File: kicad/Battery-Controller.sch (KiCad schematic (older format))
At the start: 55 parts, among them J1 Screw_Terminal_01x04 - RELAY, J2 Screw_Terminal_01x04 - COM, J3 Screw_Terminal_01x08, J4 Screw_Terminal_01x02 - Batter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, J6 Screw_Terminal_01x04 - Cells, J7 Conn_01x15_Male, J8 Conn_01x15_Female, Q1 TIP120, Q2 TIP122, Q3 TIP122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

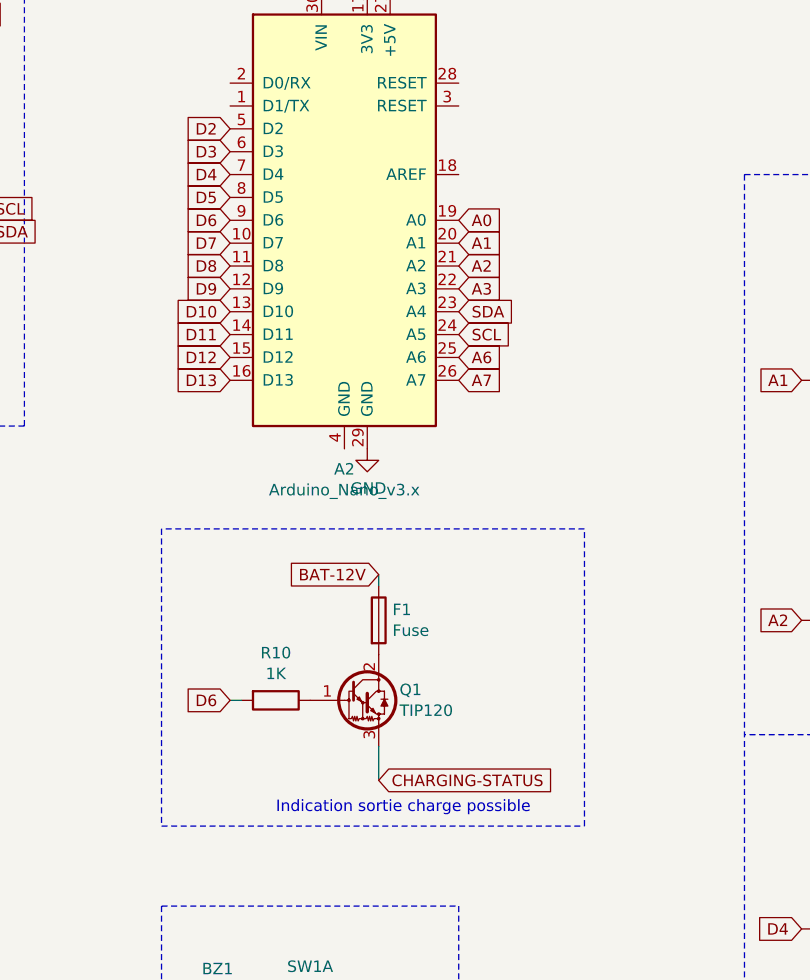
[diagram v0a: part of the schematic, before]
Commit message: Fonctionne, correctement réglé, NO serial transfer
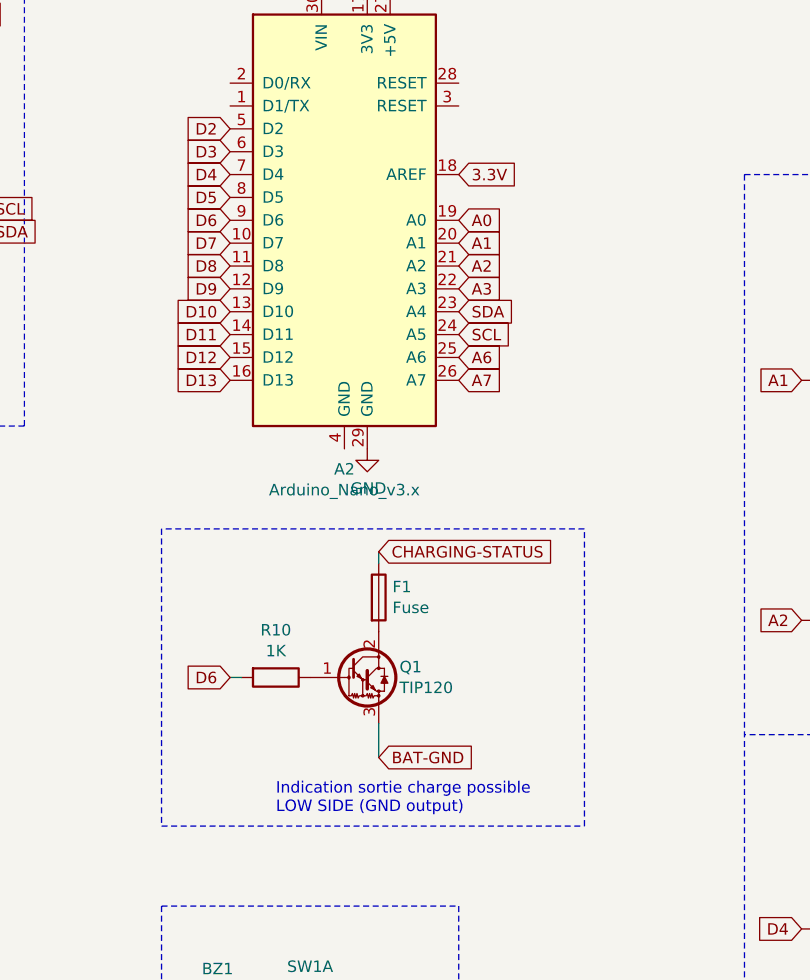
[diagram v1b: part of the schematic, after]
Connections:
- net +12V: no longer F1.1
- net 3.3V: now also A2.18 (AREF)
- net CHARGING-STATUS: now also F1.1; no longer Q1.3 (E)
- net GND: now also Q1.3 (E)
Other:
- note added: "Indication sortie charge possible\nLOW SIDE (GND output)\n"
- note removed: "Indication sortie charge possible\n"
- moved on the sheet: F1, Q1, R10
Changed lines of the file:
@@
 L Transistor_BJT:TIP120 Q1
 U 1 1 61B48AE2
-P 6750 6400
-F 0 "Q1" H 6941 6446 50  0000 L CNN
-F 1 "TIP120" H 6941 6355 50  0000 L CNN
-F 2 "Package_TO_SOT_THT:TO-220-3_Vertical" H 6950 6500 50  0001 C CNN
-F 3 "~" H 6750 6400 50  0001 C CNN
-	1    6750 6400
+P 6750 6300
+F 0 "Q1" H 6941 6346 50  0000 L CNN
+F 1 "TIP120" H 6941 6255 50  0000 L CNN
+F 2 "Package_TO_SOT_THT:TO-220-3_Vertical" H 6950 6400 50  0001 C CNN
+F 3 "~" H 6750 6300 50  0001 C CNN
+	1    6750 6300
 	1    0    0    -1
 $EndComp
@@
 L Device:R R10
 U 1 1 61B49F2F
-P 6400 6400
-F 0 "R10" V 6193 6400 50  0000 C CNN
-F 1 "1K" V 6284 6400 50  0000 C CNN
-F 2 "Resistor_THT:R_Axial_DIN0207_L6.3mm_D2.5mm_P10.16mm_Horizontal" V 6330 6400 50  0001 C CNN
-F 3 "~" H 6400 6400 50  0001 C CNN
-	1    6400 6400
+P 6400 6300
+F 0 "R10" V 6193 6300 50  0000 C CNN
+F 1 "1K" V 6284 6300 50  0000 C CNN
+F 2 "Resistor_THT:R_Axial_DIN0207_L6.3mm_D2.5mm_P10.16mm_Horizontal" V 6330 6300 50  0001 C CNN
+F 3 "~" H 6400 6300 50  0001 C CNN
+	1    6400 6300
 	0    1    1    0
 $EndComp
@@
 	5900 5650 5900 6950
 Text Notes 6400 6900 0    50   ~ 0
-Indication sortie charge possible\n
+Indication sortie charge possible\nLOW SIDE (GND output)\n
 $Comp
 L Device:Fuse F1
 U 1 1 61B5B3F4
-P 6850 6050
-F 0 "F1" H 6910 6096 50  0000 L CNN
-F 1 "Fuse" H 6910 6005 50  0000 L CNN
-F 2 "Fuse:Fuseholder_Blade_ATO_Littelfuse_Pudenz_2_Pin" V 6780 6050 50  0001 C CNN
-F 3 "~" H 6850 6050 50  0001 C CNN
-	1    6850 6050
-	1    0    0    -1
-$EndComp
-Wire Wire Line
-	6850 6600 6850 6750
-Text GLabel 6850 6750 2    50   Input ~ 0
+P 6850 5950
+F 0 "F1" H 6910 5996 50  0000 L CNN
+F 1 "Fuse" H 6910 5905 50  0000 L CNN
+F 2 "Fuse:Fuseholder_Blade_ATO_Littelfuse_Pudenz_2_Pin" V 6780 5950 50  0001 C CNN
+F 3 "~" H 6850 5950 50  0001 C CNN
+	1    6850 5950
+	1    0    0    -1
+$EndComp
+Wire Wire Line
+	6850 6500 6850 6650
+Text GLabel 6850 5750 2    50   Input ~ 0
 CHARGING-STATUS
 Wire Notes Line
@@
 Text GLabel 6200 4300 0    50   Input ~ 0
 D6
-Text GLabel 6200 6400 0    50   Input ~ 0
+Text GLabel 6200 6300 0    50   Input ~ 0
 D6
 Wire Wire Line
-	6250 6400 6200 6400
+	6250 6300 6200 6300
 $Comp
 L Connector:Screw_Terminal_01x04 J1
@@
 	1    0    0    -1
 $EndComp
-Text GLabel 6850 5850 0    50   Input ~ 0
-BAT-12V
-Wire Wire Line
-	6850 5850 6850 5900
+Text GLabel 6850 6650 2    50   Input ~ 0
+BAT-GND
+Wire Wire Line
+	6850 5750 6850 5800
 $Comp
 L yaaj_dcdc_stepdown_lm2596:YAAJ_DCDC_StepDown_LM2596 U1
@@
 Wire Wire Line
 	9400 8250 9300 8250
+Text GLabel 7200 4100 2    50   Input ~ 0
+3.3V
 $EndSCHEMATC

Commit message: RS484 included, not enough ram
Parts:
- removed BZ1: Buzzer, Buzzer_Beeper:Buzzer_12x9.5RM7.6, symbol Device:Buzzer
- removed SW1: SW_DPST_x2, Connector_PinHeader_2.54mm:PinHeader_1x02_P2.54mm_Vertical, symbol Switch:SW_DPST_x2
- added Arduino2: Arduino_Nano_v3.x, Module:Arduino_Nano, symbol Battery-Controller-rescue:Arduino_Nano_v3.x-MCU_Module
- added C?: 1.5uF, Capacitor_THT:C_Disc_D8.0mm_W5.0mm_P7.50mm, symbol Device:CP
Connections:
- net GND2: now also U4.2 (~RE), C?.2
- net UP-5V: now also C?.1
- net UP-D7: now also U4.3 (DE)
- net RS-485-OUT1 renamed RS-485-RX
- net RS-485-RX: now also U4.6 (A); no longer U4.7 (B)
- net RS-485-OUT2 renamed RS-485-TX
- net RS-485-TX: now also U4.7 (B); no longer U4.6 (A)
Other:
- note removed: "Buzzer\n"
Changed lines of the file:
@@
 Text GLabel 7200 4800 2    50   Input ~ 0
 SCL
-$Comp
-L Device:Buzzer BZ1
-U 1 1 61B2EC2C
-P 6150 7900
-F 0 "BZ1" H 6155 7575 50  0000 C CNN
-F 1 "Buzzer" H 6155 7666 50  0000 C CNN
-F 2 "Buzzer_Beeper:Buzzer_12x9.5RM7.6" V 6125 8000 50  0001 C CNN
-F 3 "~" V 6125 8000 50  0001 C CNN
-	1    6150 7900
-	-1   0    0    1
-$EndComp
-Text GLabel 6800 7800 2    50   Input ~ 0
-UP-D7
 Text GLabel 6200 4400 0    50   Input ~ 0
 D7
-$Comp
-L Switch:SW_DPST_x2 SW1
-U 1 1 61B4152C
-P 6550 7800
-F 0 "SW1" H 6550 8035 50  0000 C CNN
-F 1 "SW_DPST_x2" H 6550 7944 50  0000 C CNN
-F 2 "Connector_PinHeader_2.54mm:PinHeader_1x02_P2.54mm_Vertical" H 6550 7800 50  0001 C CNN
-F 3 "~" H 6550 7800 50  0001 C CNN
-	1    6550 7800
-	1    0    0    -1
-$EndComp
 $Comp
 L Transistor_BJT:TIP120 Q1
@@
 Text GLabel 6850 5750 2    50   Input ~ 0
 CHARGING-STATUS
-Wire Notes Line
-	7200 8250 5900 8250
-Wire Notes Line
-	5900 8250 5900 7300
-Wire Notes Line
-	5900 7300 7200 7300
-Wire Notes Line
-	7200 7300 7200 8250
-Text Notes 6850 8200 0    50   ~ 0
-Buzzer\n
 Text Notes 11350 8800 0    50   ~ 0
 LOAD relay\n
@@
 	3600 7400 3600 7350
 Wire Wire Line
-	4200 7350 3600 7350
+	4200 7350 4050 7350
 Connection ~ 3600 7350
 Text GLabel 3900 7850 2    50   Input ~ 0
-RS-485-OUT1
+RS-485-TX
 Text GLabel 3900 7950 2    50   Input ~ 0
-RS-485-OUT2
+RS-485-RX
 Text GLabel 9900 1650 0    50   Input ~ 0
-RS-485-OUT1
+RS-485-RX
 Text GLabel 9900 1750 0    50   Input ~ 0
-RS-485-OUT2
+RS-485-TX
 Text Notes 4100 8450 0    50   ~ 0
 RS-485 BUS
@@
 Text GLabel 9900 2050 0    50   Input ~ 0
 LOAD-RELAY-STATUS
-Wire Wire Line
-	6400 8000 6250 8000
-Wire Wire Line
-	6250 7800 6350 7800
-Wire Wire Line
-	6800 7800 6750 7800
 Text GLabel 9900 2550 0    50   Input ~ 0
 SOC-ENABLE
@@
 $EndComp
 $Comp
-L power:GND2 #PWR0126
-U 1 1 6214F46F
-P 3650 9550
-F 0 "#PWR0126" H 3650 9300 50  0001 C CNN
-F 1 "GND2" H 3655 9377 50  0000 C CNN
-F 2 "" H 3650 9550 50  0001 C CNN
-F 3 "" H 3650 9550 50  0001 C CNN
-	1    3650 9550
-	1    0    0    -1
-$EndComp
-Text GLabel 3400 9550 0    50   Input ~ 0
-TUP-01
-Wire Wire Line
-	3400 9550 3650 9550
-Text GLabel 3400 9350 0    50   Input ~ 0
-TUP-02
-$Comp
-L power:+5VD #PWR0127
-U 1 1 621617F9
-P 3650 9300
-F 0 "#PWR0127" H 3650 9150 50  0001 C CNN
-F 1 "+5VD" H 3665 9473 50  0000 C CNN
-F 2 "" H 3650 9300 50  0001 C CNN
-F 3 "" H 3650 9300 50  0001 C CNN
-	1    3650 9300
-	1    0    0    -1
-$EndComp
-Wire Wire Line
-	3650 9300 3650 9350
-Wire Wire Line
-	3650 9350 3400 9350
-$Comp
 L power:GND2 #PWR0136
 U 1 1 621804D7
@@
 	1    0    0    -1
 $EndComp
-$Comp
-L power:+3.3VA #PWR0139
-U 1 1 6218958A
-P 3700 10200
-F 0 "#PWR0139" H 3700 10050 50  0001 C CNN
-F 1 "+3.3VA" H 3715 10373 50  0000 C CNN
-F 2 "" H 3700 10200 50  0001 C CNN
-F 3 "" H 3700 10200 50  0001 C CNN
-	1    3700 10200
-	1    0    0    -1
-$EndComp
-Text GLabel 3400 10200 0    50   Input ~ 0
-TUP-02
-Wire Wire Line
-	3400 10200 3700 10200
 $Comp
 L power:GND2 #PWR0141
@@
 Text GLabel 14000 1150 2    50   Input ~ 0
 5V
-$Comp
-L power:GND2 #PWR0102
-U 1 1 627A7DEA
-P 6400 8000
-F 0 "#PWR0102" H 6400 7750 50  0001 C CNN
-F 1 "GND2" H 6405 7827 50  0000 C CNN
-F 2 "" H 6400 8000 50  0001 C CNN
-F 3 "" H 6400 8000 50  0001 C CNN
-	1    6400 8000
-	1    0    0    -1
-$EndComp
 Text GLabel 14000 2150 2    50   Input ~ 0
 D7
@@
 Text GLabel 7200 4100 2    50   Input ~ 0
 3.3V
+$Comp
+L Battery-Controller-rescue:Arduino_Nano_v3.x-MCU_Module Arduino2
+U 1 1 61D0DBA8
+P 14950 6750
+F 0 "Arduino2" H 14950 5661 50  0000 C CNN
+F 1 "Arduino_Nano_v3.x" H 14950 5570 50  0000 C CNN
+F 2 "Module:Arduino_Nano" H 15100 5800 50  0001 L CNN
+F 3 "http://www.mouser.com/pdfdocs/Gravitech_Arduino_Nano3_0.pdf" H 14950 5750 50  0001 C CNN
+	1    14950 6750
+	1    0    0    -1
+$EndComp
+Connection ~ 4050 7350
+Wire Wire Line
+	4050 7350 3600 7350
+$Comp
+L Device:CP C?
+U 1 1 61D104DE
+P 4050 7500
+F 0 "C?" H 4168 7546 50  0000 L CNN
+F 1 "1.5uF" H 4168 7455 50  0000 L CNN
+F 2 "Capacitor_THT:C_Disc_D8.0mm_W5.0mm_P7.50mm" H 4088 7350 50  0001 C CNN
+F 3 "~" H 4050 7500 50  0001 C CNN
+	1    4050 7500
+	1    0    0    -1
+$EndComp
+$Comp
+L power:GND2 #PWR?
+U 1 1 61D14DB0
+P 4550 7650
+F 0 "#PWR?" H 4550 7400 50  0001 C CNN
+F 1 "GND2" H 4555 7477 50  0000 C CNN
+F 2 "" H 4550 7650 50  0001 C CNN
+F 3 "" H 4550 7650 50  0001 C CNN
+	1    4550 7650
+	1    0    0    -1
+$EndComp
+Wire Wire Line
+	4550 7650 4050 7650
+Text GLabel 3300 7550 0    50   Input ~ 0
+UP-D7
+$Comp
+L power:GND2 #PWR?
+U 1 1 61D19D1C
+P 3150 8150
+F 0 "#PWR?" H 3150 7900 50  0001 C CNN
+F 1 "GND2" H 3155 7977 50  0000 C CNN
+F 2 "" H 3150 8150 50  0001 C CNN
+F 3 "" H 3150 8150 50  0001 C CNN
+	1    3150 8150
+	1    0    0    -1
+$EndComp
+Wire Wire Line
+	3150 8150 3150 7850
+Wire Wire Line
+	3150 7850 3300 7850
 $EndSCHEMATC
